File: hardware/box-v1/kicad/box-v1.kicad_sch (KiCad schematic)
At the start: 0 parts

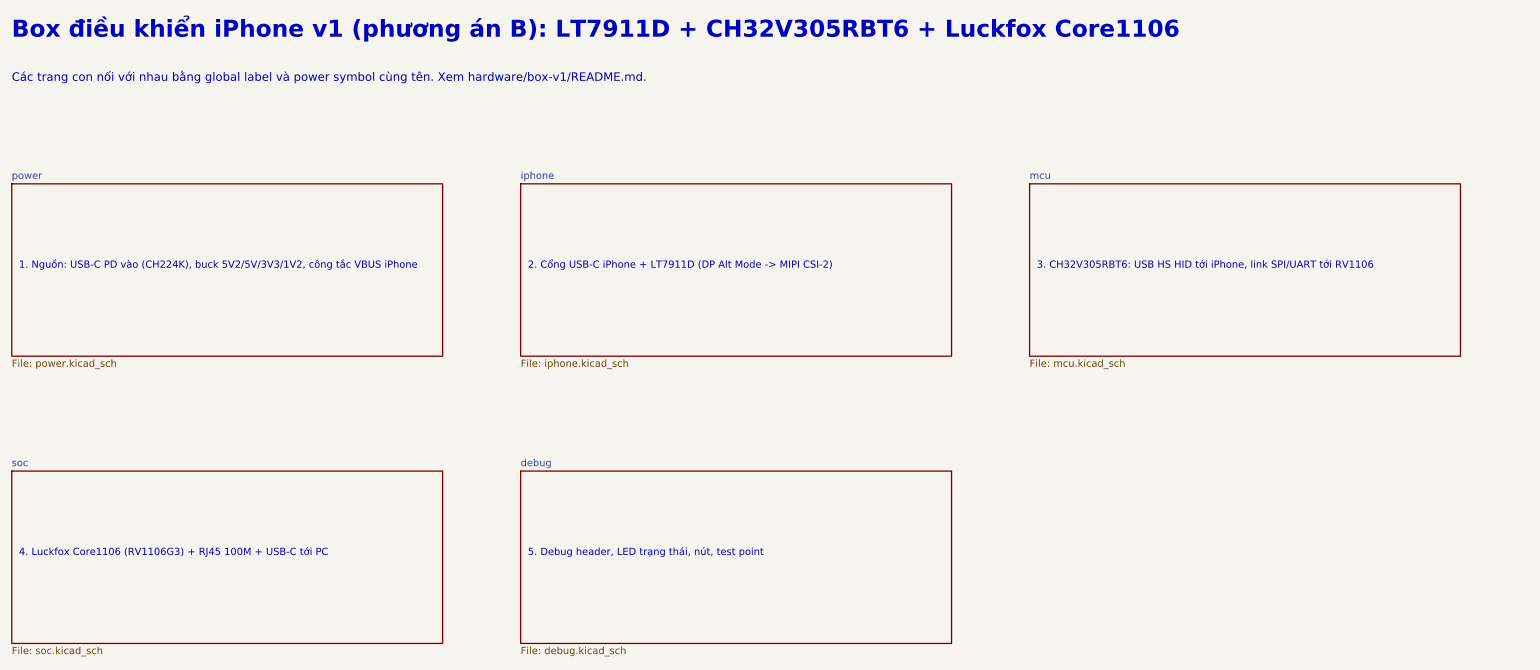
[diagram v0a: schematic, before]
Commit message: hardware/box-v1 in English, with an order package
- Everything in hardware/box-v1 is English: netlist.py, the generators,
  the checks, the README, and the regenerated KiCad sheets, SVGs, BOM
  and netlists. Labels are Confirmed / Likely / Unknown; Option A/B.
- netlist.py carries the ordering data of every BOM line: manufacturer,
  MPN, LCSC code with its evidence, JLCPCB class, price estimate, how it
  is assembled. bom.csv has the new columns; check.py rule R11 checks
  them and the selftest plants 12 faults.
- ORDERING.md: what to send a layout and assembly house, what is done
  and what the vendor does (the layout), the LT7911D documents to ask
  Lontium for, fabrication and assembly specs, bring-up tests, cost
  estimates at 10 and 50 boards, and an RFQ template.
- mechanical.py draws the enclosure outline and connector openings
  (svg/mechanical.svg).
- Design fixes: NRST note (4.7k), the end-of-life inductor replaced
  (SRP1038A-100M), the Bob-Smith capacitor rated 2 kV, capacitor ratings
  matched to stocked parts. Open points are listed in the README.

Co-Authored-By: Claude Opus 5.5 <noreply@anthropic.com>
Claude-Session: https://claude.ai/code/session_01EUDgAy5nU6wYzfaiaKBwjy
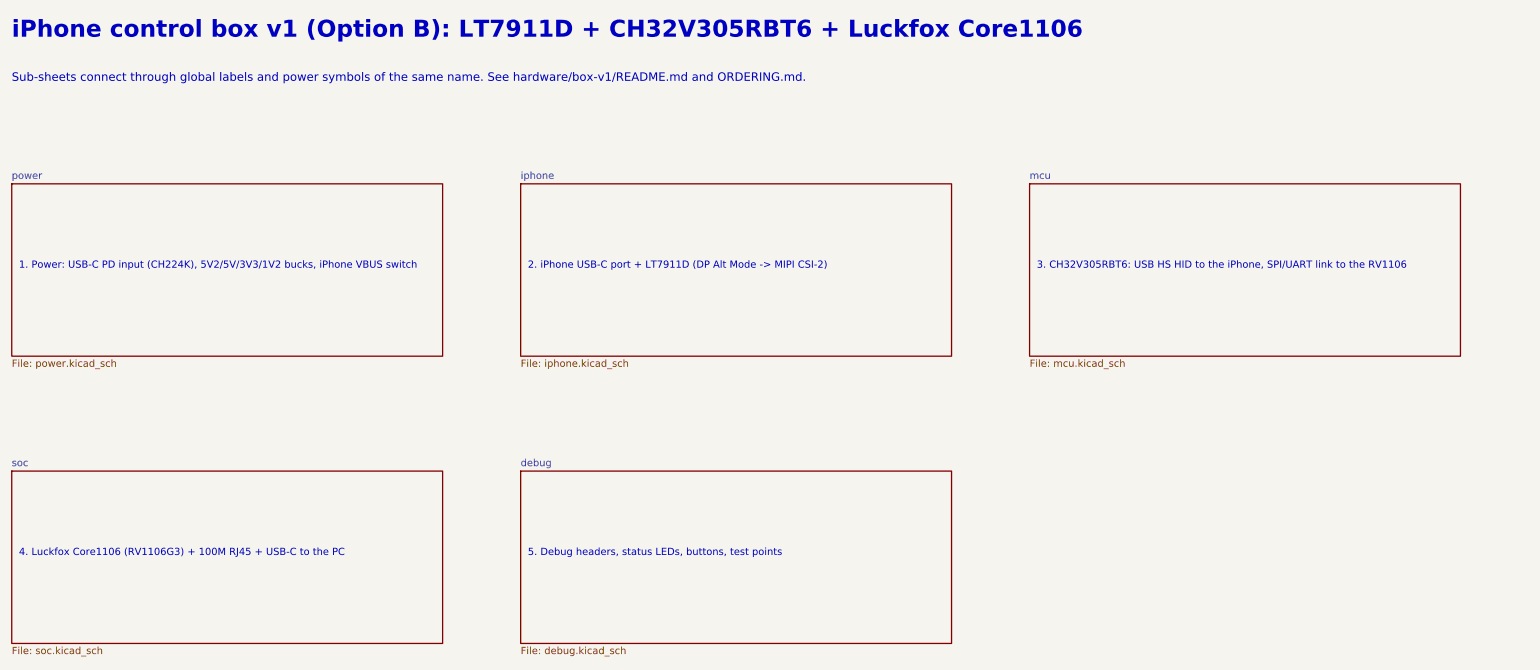
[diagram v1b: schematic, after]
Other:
- note added: "1. Power: USB-C PD input (CH224K), 5V2/5V/3V3/1V2 bucks, iPhone VBUS switch"
- note added: "2. iPhone USB-C port + LT7911D (DP Alt Mode -> MIPI CSI-2)"
- note added: "3. CH32V305RBT6: USB HS HID to the iPhone, SPI/UART link to the RV1106"
- note added: "4. Luckfox Core1106 (RV1106G3) + 100M RJ45 + USB-C to the PC"
- note added: "5. Debug headers, status LEDs, buttons, test points"
- note added: "Sub-sheets connect through global labels and power symbols of the same name. See hardware/box-v1/README.md and ORDERING.md."
- note added: "iPhone control box v1 (Option B): LT7911D + CH32V305RBT6 + Luckfox Core1106"
- note removed: "1. Nguồn: USB-C PD vào (CH224K), buck 5V2/5V/3V3/1V2, công tắc VBUS iPhone"
- note removed: "2. Cổng USB-C iPhone + LT7911D (DP Alt Mode -> MIPI CSI-2)"
- note removed: "3. CH32V305RBT6: USB HS HID tới iPhone, link SPI/UART tới RV1106"
- note removed: "4. Luckfox Core1106 (RV1106G3) + RJ45 100M + USB-C tới PC"
- note removed: "5. Debug header, LED trạng thái, nút, test point"
- note removed: "Box điều khiển iPhone v1 (phương án B): LT7911D + CH32V305RBT6 + Luckfox Core1106"
- note removed: "Các trang con nối với nhau bằng global label và power symbol cùng tên. Xem hardware/box-v1/README.md."
- title: box-v1: sơ đồ tổng -> box-v1: top sheet
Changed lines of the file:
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@@
 	(paper "A4")
 	(title_block
-		(title "box-v1: sơ đồ tổng")
+		(title "box-v1: top sheet")
 		(date "2026-09-26")
 		(rev "v1")
 		(company "iphone-hid / hardware/box-v1")
-		(comment 1 "Sinh từ netlist.py bằng generate.py; sửa netlist.py, không sửa file này")
-		(comment 2 "Số chân '?..' = [Chưa biết], phải xác nhận trước khi layout")
-		(comment 3 "Trang 1/6")
-	)
-	(text "Box điều khiển iPhone v1 (phương án B): LT7911D + CH32V305RBT6 + Luckfox Core1106"
+		(comment 1 "Generated from netlist.py by generate.py; edit netlist.py, not this file")
+		(comment 2 "Pin numbers '?..' = [Unknown], must be confirmed before layout")
+		(comment 3 "Sheet 1/6")
+	)
+	(text "iPhone control box v1 (Option B): LT7911D + CH32V305RBT6 + Luckfox Core1106"
 		(exclude_from_sim no)
 		(at 20.32 25.4 0)
@@
 		)
 	)
-	(text "Các trang con nối với nhau bằng global label và power symbol cùng tên. Xem hardware/box-v1/README.md."
+	(text "Sub-sheets connect through global labels and power symbols of the same name. See hardware/box-v1/README.md and ORDERING.md."
 		(exclude_from_sim no)
 		(at 20.32 33.02 0)
@@
 		)
 	)
-	(text "1. Nguồn: USB-C PD vào (CH224K), buck 5V2/5V/3V3/1V2, công tắc VBUS iPhone"
+	(text "1. Power: USB-C PD input (CH224K), 5V2/5V/3V3/1V2 bucks, iPhone VBUS switch"
 		(exclude_from_sim no)
 		(at 21.59 66.04 0)
@@
 		)
 	)
-	(text "2. Cổng USB-C iPhone + LT7911D (DP Alt Mode -> MIPI CSI-2)"
+	(text "2. iPhone USB-C port + LT7911D (DP Alt Mode -> MIPI CSI-2)"
 		(exclude_from_sim no)
 		(at 111.59 66.04 0)
@@
 		)
 	)
-	(text "3. CH32V305RBT6: USB HS HID tới iPhone, link SPI/UART tới RV1106"
+	(text "3. CH32V305RBT6: USB HS HID to the iPhone, SPI/UART link to the RV1106"
 		(exclude_from_sim no)
 		(at 201.59 66.04 0)
@@
 		)
 	)
-	(text "4. Luckfox Core1106 (RV1106G3) + RJ45 100M + USB-C tới PC"
+	(text "4. Luckfox Core1106 (RV1106G3) + 100M RJ45 + USB-C to the PC"
 		(exclude_from_sim no)
 		(at 21.59 116.84 0)
@@
 		)
 	)
-	(text "5. Debug header, LED trạng thái, nút, test point"
+	(text "5. Debug headers, status LEDs, buttons, test points"
 		(exclude_from_sim no)
 		(at 111.59 116.84 0)
